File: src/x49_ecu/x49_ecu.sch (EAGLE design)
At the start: 13 parts, among them J1 1-776163-4, J2 DTP13-4P

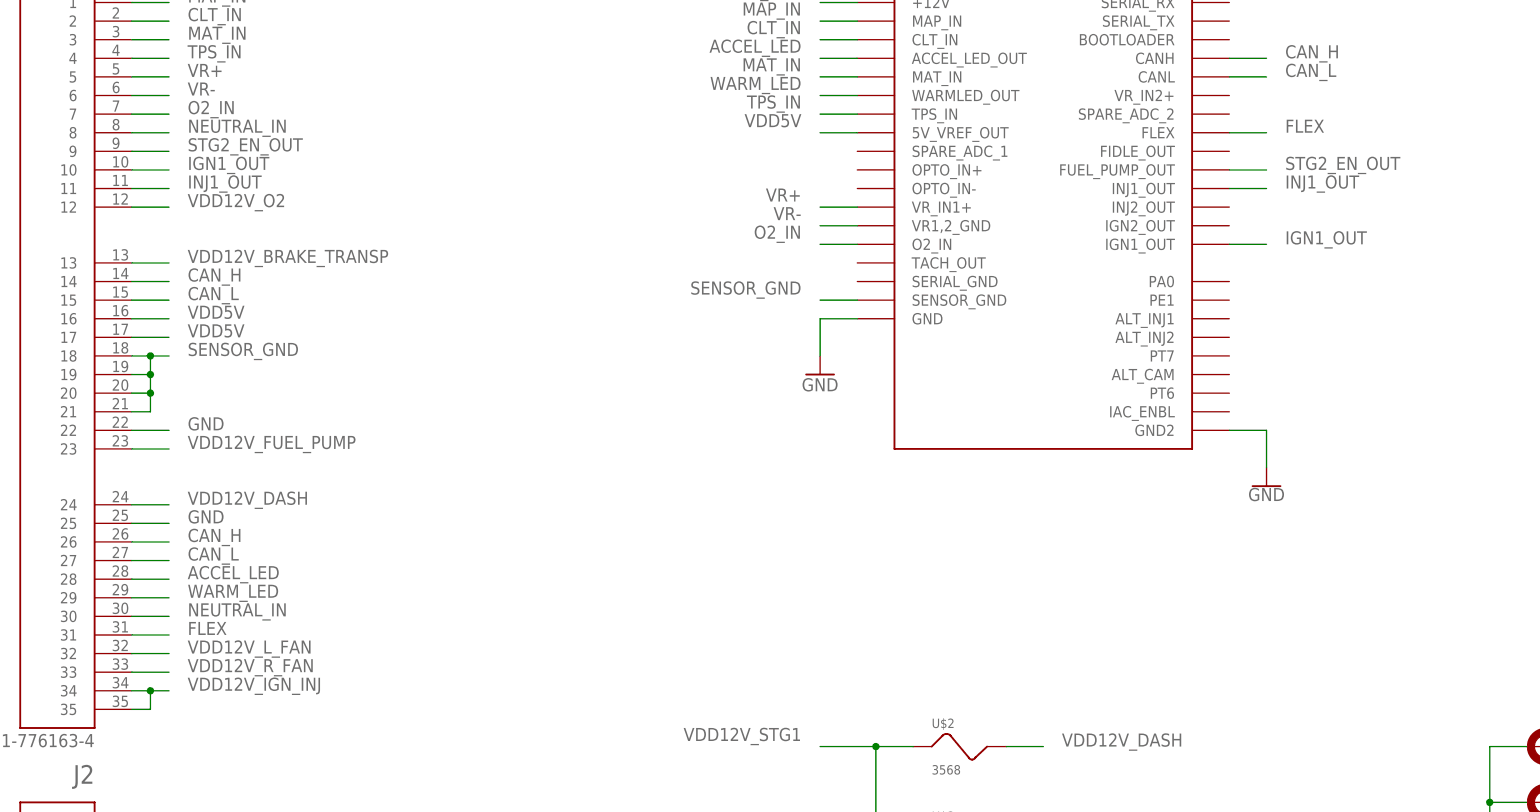
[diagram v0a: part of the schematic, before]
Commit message: x49_ecu: Connect fan supply to MS FIDLE
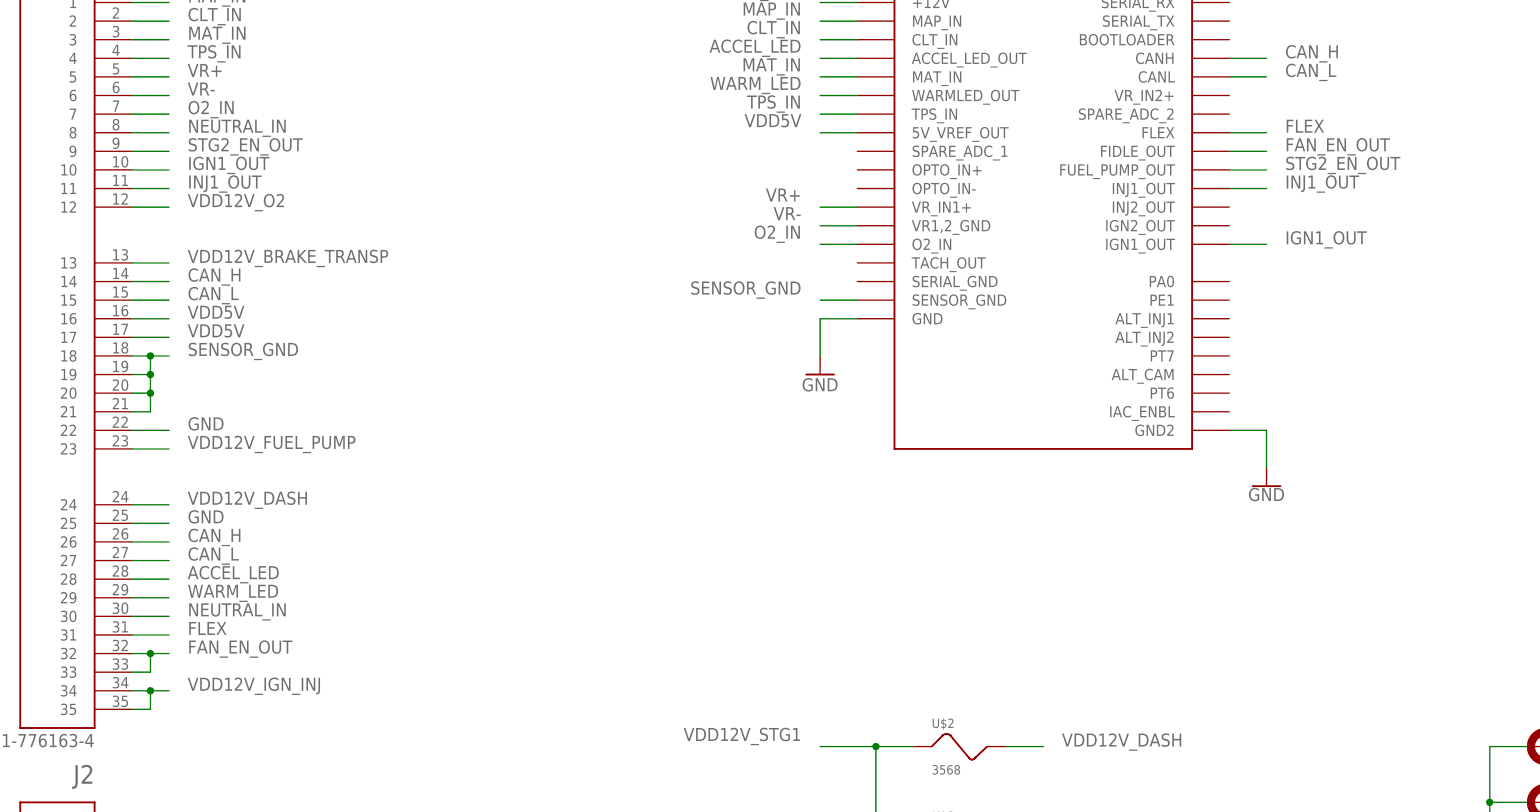
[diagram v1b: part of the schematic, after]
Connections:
- removed net VDD12V_L_FAN: J1.32
- removed net VDD12V_R_FAN: J1.33
- new net FAN_EN_OUT: J1.32, J1.33, MICROSQUIRT.FIDLE_OUT
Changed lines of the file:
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@@
 <setting verticaltext="up"/>
 </settings>
-<grid distance="0.1" unitdist="inch" unit="inch" style="lines" multiple="1" display="no" altdistance="0.01" altunitdist="inch" altunit="inch"/>
+<grid distance="0.1" unitdist="inch" unit="inch" style="lines" multiple="1" display="yes" altdistance="0.01" altunitdist="inch" altunit="inch"/>
 <layers>
 <layer number="1" name="Top" color="4" fill="1" visible="no" active="no"/>
@@
 </segment>
 </net>
-<net name="VDD12V_L_FAN" class="0">
-<segment>
-<pinref part="J1" gate="G$1" pin="32"/>
-<wire x1="20.32" y1="12.7" x2="25.4" y2="12.7" width="0.1524" layer="91"/>
-<label x="27.94" y="12.7" size="1.778" layer="95"/>
-</segment>
-</net>
-<net name="VDD12V_R_FAN" class="0">
-<segment>
-<pinref part="J1" gate="G$1" pin="33"/>
-<wire x1="20.32" y1="10.16" x2="25.4" y2="10.16" width="0.1524" layer="91"/>
-<label x="27.94" y="10.16" size="1.778" layer="95"/>
-</segment>
-</net>
 <net name="NEUTRAL_IN" class="0">
 <segment>
@@
 </segment>
 </net>
+<net name="FAN_EN_OUT" class="0">
+<segment>
+<pinref part="MICROSQUIRT" gate="G$1" pin="FIDLE_OUT"/>
+<wire x1="170.18" y1="81.28" x2="175.26" y2="81.28" width="0.1524" layer="91"/>
+<label x="177.8" y="81.28" size="1.778" layer="95"/>
+</segment>
+<segment>
+<pinref part="J1" gate="G$1" pin="32"/>
+<wire x1="20.32" y1="12.7" x2="22.86" y2="12.7" width="0.1524" layer="91"/>
+<label x="27.94" y="12.7" size="1.778" layer="95"/>
+<pinref part="J1" gate="G$1" pin="33"/>
+<wire x1="22.86" y1="12.7" x2="25.4" y2="12.7" width="0.1524" layer="91"/>
+<wire x1="20.32" y1="10.16" x2="22.86" y2="10.16" width="0.1524" layer="91"/>
+<wire x1="22.86" y1="10.16" x2="22.86" y2="12.7" width="0.1524" layer="91"/>
+<junction x="22.86" y="12.7"/>
+</segment>
+</net>

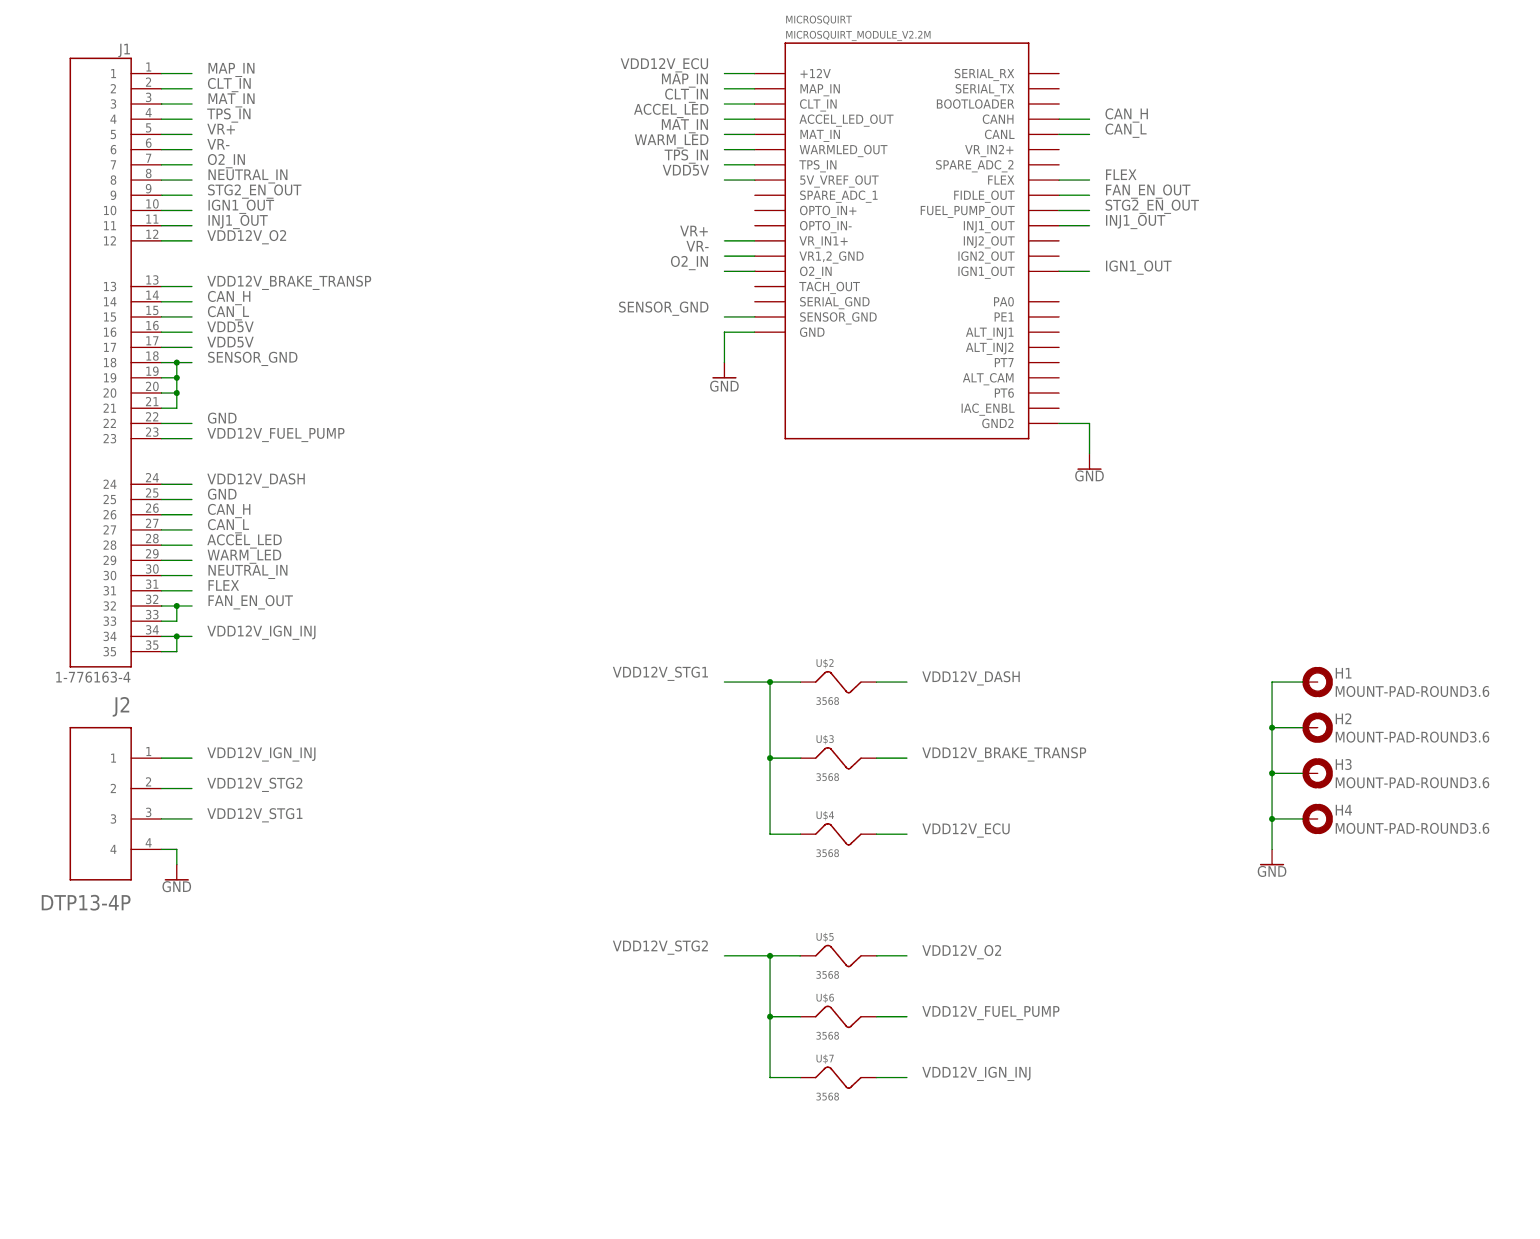
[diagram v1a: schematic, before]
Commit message: x49_ecu: revision 1a with second DTP connector
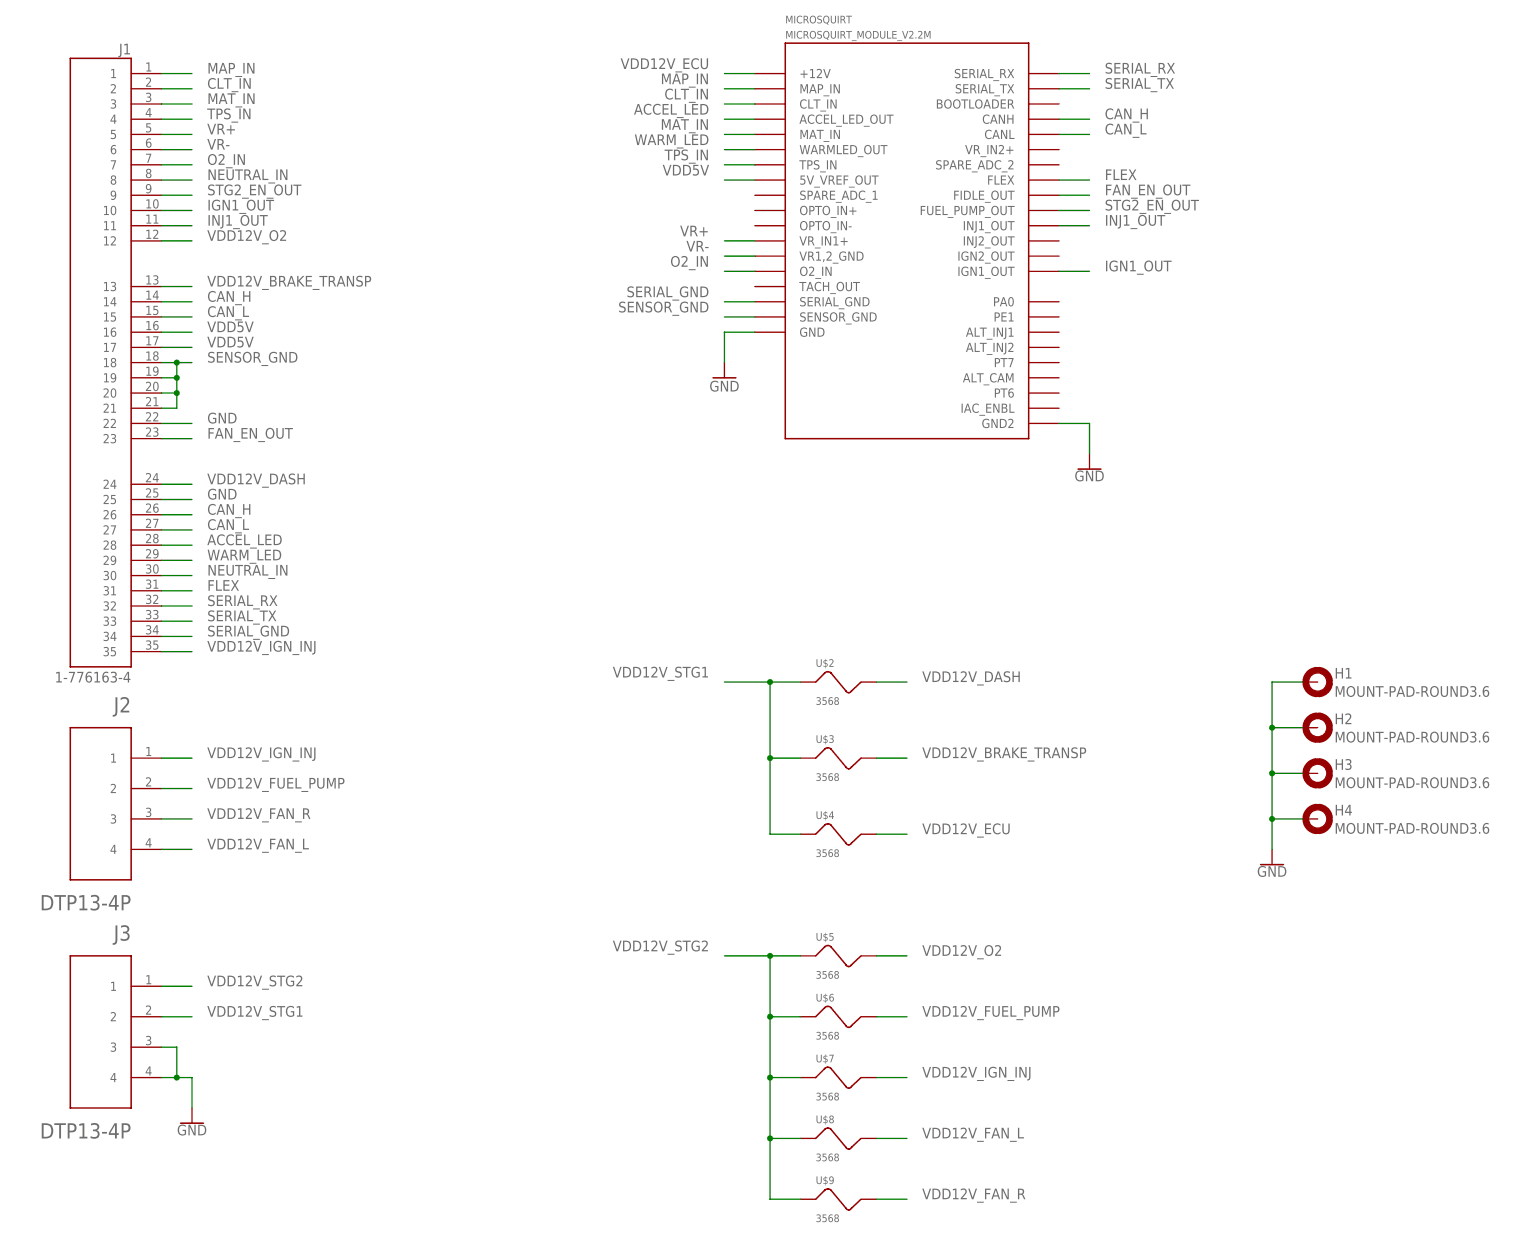
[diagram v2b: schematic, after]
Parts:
- added J3: DTP13-4P, te_connectivity:DTP13-4P
- added U$8, U$9: 3568, keystone_electronics:3568
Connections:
- new net SERIAL_GND: J1.34, MICROSQUIRT.SERIAL_GND
- new net SERIAL_RX: J1.32, MICROSQUIRT.SERIAL_RX
- new net SERIAL_TX: J1.33, MICROSQUIRT.SERIAL_TX
- new net VDD12V_FAN_L: J2.4, U$8.2
- new net VDD12V_FAN_R: J2.3, U$9.2
- net FAN_EN_OUT: now also J1.23; no longer J1.32, J1.33
- net GND: now also J3.3, J3.4; no longer J2.4
- net VDD12V_FUEL_PUMP: now also J2.2; no longer J1.23
- net VDD12V_IGN_INJ: no longer J1.34
- net VDD12V_STG1: now also J3.2; no longer J2.3
- net VDD12V_STG2: now also J3.1, U$8.1, U$9.1; no longer J2.2

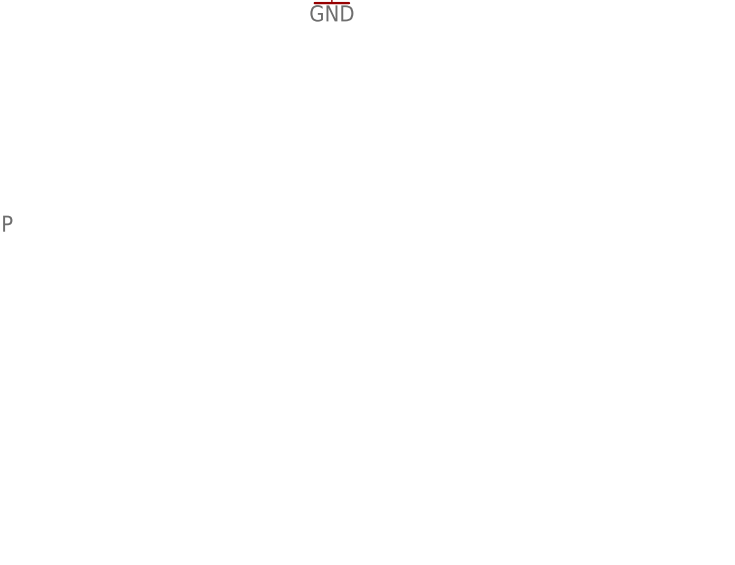
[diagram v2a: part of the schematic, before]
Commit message: x49_ecu: 1C with status LEDs
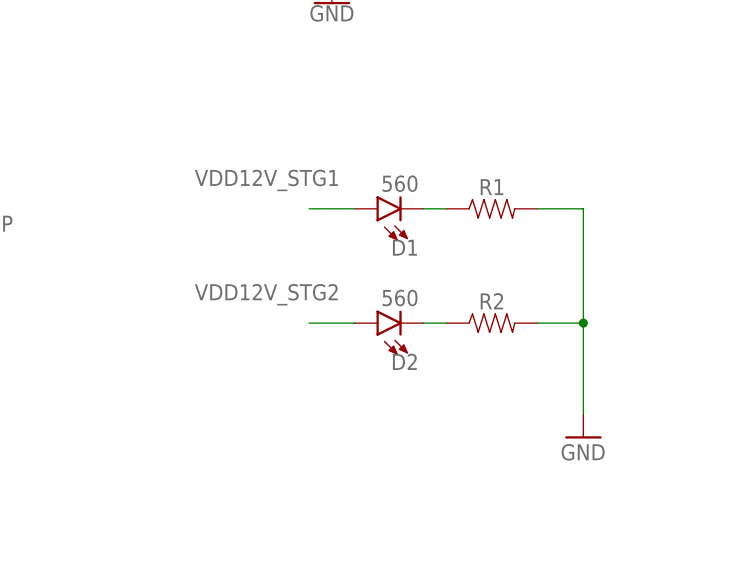
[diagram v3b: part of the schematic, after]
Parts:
- added D1, D2: 560, SparkFun-LED:LED5MM
- added R1, R2: (no value), SparkFun-Resistors:RESISTORAXIAL-0.3
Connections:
- new net N$1: D1.C, R1.1
- new net N$2: D2.C, R2.1
- net GND: now also R1.2, R2.2
- net VDD12V_STG1: now also D1.A
- net VDD12V_STG2: now also D2.A
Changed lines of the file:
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@@
 <setting verticaltext="up"/>
 </settings>
-<grid distance="0.1" unitdist="inch" unit="inch" style="lines" multiple="1" display="no" altdistance="0.01" altunitdist="inch" altunit="inch"/>
+<grid distance="0.1" unitdist="inch" unit="inch" style="lines" multiple="1" display="yes" altdistance="0.01" altunitdist="inch" altunit="inch"/>
 <layers>
 <layer number="1" name="Top" color="4" fill="1" visible="no" active="no"/>
@@
 <layer number="230" name="230bmp" color="7" fill="1" visible="yes" active="yes"/>
 <layer number="231" name="231bmp" color="7" fill="1" visible="yes" active="yes"/>
+<layer number="232" name="Eagle3D_PG2" color="7" fill="1" visible="yes" active="yes"/>
+<layer number="233" name="Eagle3D_PG3" color="7" fill="1" visible="yes" active="yes"/>
 <layer number="248" name="Housing" color="7" fill="1" visible="yes" active="yes"/>
 <layer number="249" name="Edge" color="7" fill="1" visible="yes" active="yes"/>
@@
 <part name="U$8" library="keystone_electronics" deviceset="3568" device=""/>
 <part name="U$9" library="keystone_electronics" deviceset="3568" device=""/>
+<part name="D1" library="SparkFun-LED" library_urn="urn:adsk.eagle:library:529" deviceset="LED" device="5MM" package3d_urn="urn:adsk.eagle:package:39353/1" value="560"/>
+<part name="D2" library="SparkFun-LED" library_urn="urn:adsk.eagle:library:529" deviceset="LED" device="5MM" package3d_urn="urn:adsk.eagle:package:39353/1" value="560"/>
+<part name="GND4" library="supply1" library_urn="urn:adsk.eagle:library:371" deviceset="GND" device=""/>
+<part name="R1" library="SparkFun-Resistors" library_urn="urn:adsk.eagle:library:532" deviceset="RESISTOR" device="AXIAL-0.3" package3d_urn="urn:adsk.eagle:package:39658/1" value=" "/>
+<part name="R2" library="SparkFun-Resistors" library_urn="urn:adsk.eagle:library:532" deviceset="RESISTOR" device="AXIAL-0.3" package3d_urn="urn:adsk.eagle:package:39658/1" value=" "/>
 </parts>
 <sheets>
@@
 <attribute name="NAME" x="129.54" y="-83.82" size="1.27" layer="95"/>
 <attribute name="VALUE" x="129.54" y="-90.17" size="1.27" layer="96"/>
+</instance>
+<instance part="D1" gate="G$1" x="210.82" y="-53.34" smashed="yes" rot="R90">
+<attribute name="NAME" x="215.392" y="-56.769" size="1.778" layer="95" font="vector" rot="R180"/>
+<attribute name="VALUE" x="215.392" y="-51.435" size="1.778" layer="96" font="vector" rot="R180" align="top-left"/>
+</instance>
+<instance part="D2" gate="G$1" x="210.82" y="-66.04" smashed="yes" rot="R90">
+<attribute name="NAME" x="215.392" y="-69.469" size="1.778" layer="95" font="vector" rot="R180"/>
+<attribute name="VALUE" x="215.392" y="-64.135" size="1.778" layer="96" font="vector" rot="R180" align="top-left"/>
+</instance>
+<instance part="GND4" gate="1" x="233.68" y="-78.74" smashed="yes">
+<attribute name="VALUE" x="231.14" y="-81.28" size="1.778" layer="96"/>
+</instance>
+<instance part="R1" gate="G$1" x="223.52" y="-53.34" smashed="yes">
+<attribute name="NAME" x="223.52" y="-51.816" size="1.778" layer="95" font="vector" align="bottom-center"/>
+<attribute name="VALUE" x="223.52" y="-54.864" size="1.778" layer="96" font="vector" align="top-center"/>
+</instance>
+<instance part="R2" gate="G$1" x="223.52" y="-66.04" smashed="yes">
+<attribute name="NAME" x="223.52" y="-64.516" size="1.778" layer="95" font="vector" align="bottom-center"/>
+<attribute name="VALUE" x="223.52" y="-67.564" size="1.778" layer="96" font="vector" align="top-center"/>
 </instance>
 </instances>
@@
 <wire x1="25.4" y1="-66.04" x2="25.4" y2="-71.12" width="0.1524" layer="91"/>
 <pinref part="GND1" gate="1" pin="GND"/>
+</segment>
+<segment>
+<pinref part="R2" gate="G$1" pin="2"/>
+<pinref part="GND4" gate="1" pin="GND"/>
+<wire x1="228.6" y1="-66.04" x2="233.68" y2="-66.04" width="0.1524" layer="91"/>
+<wire x1="233.68" y1="-66.04" x2="233.68" y2="-76.2" width="0.1524" layer="91"/>
+<pinref part="R1" gate="G$1" pin="2"/>
+<wire x1="228.6" y1="-53.34" x2="233.68" y2="-53.34" width="0.1524" layer="91"/>
+<wire x1="233.68" y1="-53.34" x2="233.68" y2="-66.04" width="0.1524" layer="91"/>
+<junction x="233.68" y="-66.04"/>
 </segment>
 </net>
@@
 <label x="27.94" y="-50.8" size="1.778" layer="95"/>
 </segment>
+<segment>
+<pinref part="D2" gate="G$1" pin="A"/>
+<wire x1="208.28" y1="-66.04" x2="203.2" y2="-66.04" width="0.1524" layer="91"/>
+<label x="190.5" y="-63.5" size="1.778" layer="95"/>
+</segment>
 </net>
 <net name="VDD12V_IGN_INJ" class="1">
@@
 <wire x1="20.32" y1="-55.88" x2="25.4" y2="-55.88" width="0.1524" layer="91"/>
 <label x="27.94" y="-55.88" size="1.778" layer="95"/>
+</segment>
+<segment>
+<pinref part="D1" gate="G$1" pin="A"/>
+<wire x1="208.28" y1="-53.34" x2="203.2" y2="-53.34" width="0.1524" layer="91"/>
+<label x="190.5" y="-50.8" size="1.778" layer="95"/>
 </segment>
 </net>
@@
 </segment>
 </net>
+<net name="N$1" class="0">
+<segment>
+<pinref part="D1" gate="G$1" pin="C"/>
+<pinref part="R1" gate="G$1" pin="1"/>
+<wire x1="215.9" y1="-53.34" x2="218.44" y2="-53.34" width="0.1524" layer="91"/>
+</segment>
+</net>
+<net name="N$2" class="0">
+<segment>
+<pinref part="D2" gate="G$1" pin="C"/>
+<pinref part="R2" gate="G$1" pin="1"/>
+<wire x1="215.9" y1="-66.04" x2="218.44" y2="-66.04" width="0.1524" layer="91"/>
+</segment>
+</net>
